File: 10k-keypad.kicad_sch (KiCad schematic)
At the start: 59 parts, among them J1 AVR-ISP-6, K1 SW_Push, K10 SW_Push, K2 SW_Push, K3 SW_Push, K4 SW_Push, K5 SW_Push, K6 SW_Push, K7 SW_Push, K8 SW_Push, K9 SW_Push, SW1 SW_Push, U1 ATmega16U2-A, U2 DRV5055A2xDBZxQ1, U3 DRV5055A2xDBZxQ1, U4 DRV5055A2xDBZxQ1, U5 DRV5055A2xDBZxQ1, U6 DRV5055A2xDBZxQ1, Y1 Crystal_GND24_Small

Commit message: hall sensor circuitry
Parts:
- C10, C11, C12, C13, C14, C15, C5, C6, C7, C9: footprint (none) -> Capacitor_SMD:C_0805_2012Metric_Pad1.18x1.45mm_HandSolder
- K10, K6, K7, K8, K9: footprint marbastlib-mx:SW_MX_HS_CPG151101S11_1u -> Hall:SW_MX_HS_CPG151101S11_1u_no_center_piece
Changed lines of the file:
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@@
       (effects (font (size 1.27 1.27)))
     )
-    (property "Footprint" "" (at 67.31 45.72 0)
+    (property "Footprint" "Capacitor_SMD:C_0805_2012Metric_Pad1.18x1.45mm_HandSolder" (at 67.31 45.72 0)
       (effects (font (size 1.27 1.27)) hide)
     )
@@
       (effects (font (size 1.27 1.27)))
     )
-    (property "Footprint" "" (at 149.86 24.13 0)
+    (property "Footprint" "Capacitor_SMD:C_0805_2012Metric_Pad1.18x1.45mm_HandSolder" (at 149.86 24.13 0)
       (effects (font (size 1.27 1.27)) hide)
     )
@@
       (effects (font (size 1.27 1.27)))
     )
-    (property "Footprint" "" (at 123.19 45.72 0)
+    (property "Footprint" "Capacitor_SMD:C_0805_2012Metric_Pad1.18x1.45mm_HandSolder" (at 123.19 45.72 0)
       (effects (font (size 1.27 1.27)) hide)
     )
@@
       (effects (font (size 1.27 1.27)) hide)
     )
-    (property "Footprint" "marbastlib-mx:SW_MX_HS_CPG151101S11_1u" (at 96.52 123.19 0)
+    (property "Footprint" "Hall:SW_MX_HS_CPG151101S11_1u_no_center_piece" (at 96.52 123.19 0)
       (effects (font (size 1.27 1.27)) hide)
     )
@@
       (effects (font (size 1.27 1.27)) hide)
     )
-    (property "Footprint" "marbastlib-mx:SW_MX_HS_CPG151101S11_1u" (at 66.04 123.19 0)
+    (property "Footprint" "Hall:SW_MX_HS_CPG151101S11_1u_no_center_piece" (at 66.04 123.19 0)
       (effects (font (size 1.27 1.27)) hide)
     )
@@
       (effects (font (size 1.27 1.27)))
     )
-    (property "Footprint" "" (at 38.1 24.13 0)
+    (property "Footprint" "Capacitor_SMD:C_0805_2012Metric_Pad1.18x1.45mm_HandSolder" (at 38.1 24.13 0)
       (effects (font (size 1.27 1.27)) hide)
     )
@@
       (effects (font (size 1.27 1.27)))
     )
-    (property "Footprint" "" (at 39.37 45.72 0)
+    (property "Footprint" "Capacitor_SMD:C_0805_2012Metric_Pad1.18x1.45mm_HandSolder" (at 39.37 45.72 0)
       (effects (font (size 1.27 1.27)) hide)
     )
@@
       (effects (font (size 1.27 1.27)))
     )
-    (property "Footprint" "" (at 121.92 24.13 0)
+    (property "Footprint" "Capacitor_SMD:C_0805_2012Metric_Pad1.18x1.45mm_HandSolder" (at 121.92 24.13 0)
       (effects (font (size 1.27 1.27)) hide)
     )
@@
       (effects (font (size 1.27 1.27)))
     )
-    (property "Footprint" "" (at 151.13 45.72 0)
+    (property "Footprint" "Capacitor_SMD:C_0805_2012Metric_Pad1.18x1.45mm_HandSolder" (at 151.13 45.72 0)
       (effects (font (size 1.27 1.27)) hide)
     )
@@
       (effects (font (size 1.27 1.27)) hide)
     )
-    (property "Footprint" "marbastlib-mx:SW_MX_HS_CPG151101S11_1u" (at 50.8 123.19 0)
+    (property "Footprint" "Hall:SW_MX_HS_CPG151101S11_1u_no_center_piece" (at 50.8 123.19 0)
       (effects (font (size 1.27 1.27)) hide)
     )
@@
       (effects (font (size 1.27 1.27)))
     )
-    (property "Footprint" "" (at 93.98 24.13 0)
+    (property "Footprint" "Capacitor_SMD:C_0805_2012Metric_Pad1.18x1.45mm_HandSolder" (at 93.98 24.13 0)
       (effects (font (size 1.27 1.27)) hide)
     )
@@
       (effects (font (size 1.27 1.27)) hide)
     )
-    (property "Footprint" "marbastlib-mx:SW_MX_HS_CPG151101S11_1u" (at 35.56 123.19 0)
+    (property "Footprint" "Hall:SW_MX_HS_CPG151101S11_1u_no_center_piece" (at 35.56 123.19 0)
       (effects (font (size 1.27 1.27)) hide)
     )
@@
       (effects (font (size 1.27 1.27)))
     )
-    (property "Footprint" "" (at 66.04 24.13 0)
+    (property "Footprint" "Capacitor_SMD:C_0805_2012Metric_Pad1.18x1.45mm_HandSolder" (at 66.04 24.13 0)
       (effects (font (size 1.27 1.27)) hide)
     )
@@
       (effects (font (size 1.27 1.27)) hide)
     )
-    (property "Footprint" "marbastlib-mx:SW_MX_HS_CPG151101S11_1u" (at 81.28 123.19 0)
+    (property "Footprint" "Hall:SW_MX_HS_CPG151101S11_1u_no_center_piece" (at 81.28 123.19 0)
       (effects (font (size 1.27 1.27)) hide)
     )
@@
       (effects (font (size 1.27 1.27)))
     )
-    (property "Footprint" "" (at 95.25 45.72 0)
-      (effects (font (size 1.27 1.27)) hide)
-    )
+    (property "Footprint" "Capacitor_SMD:C_0805_2012Metric_Pad1.18x1.45mm_HandSolder" (at 95.25 45.72 0)
+      (effects (font (size 1.27 1.27)) hide)
+    )

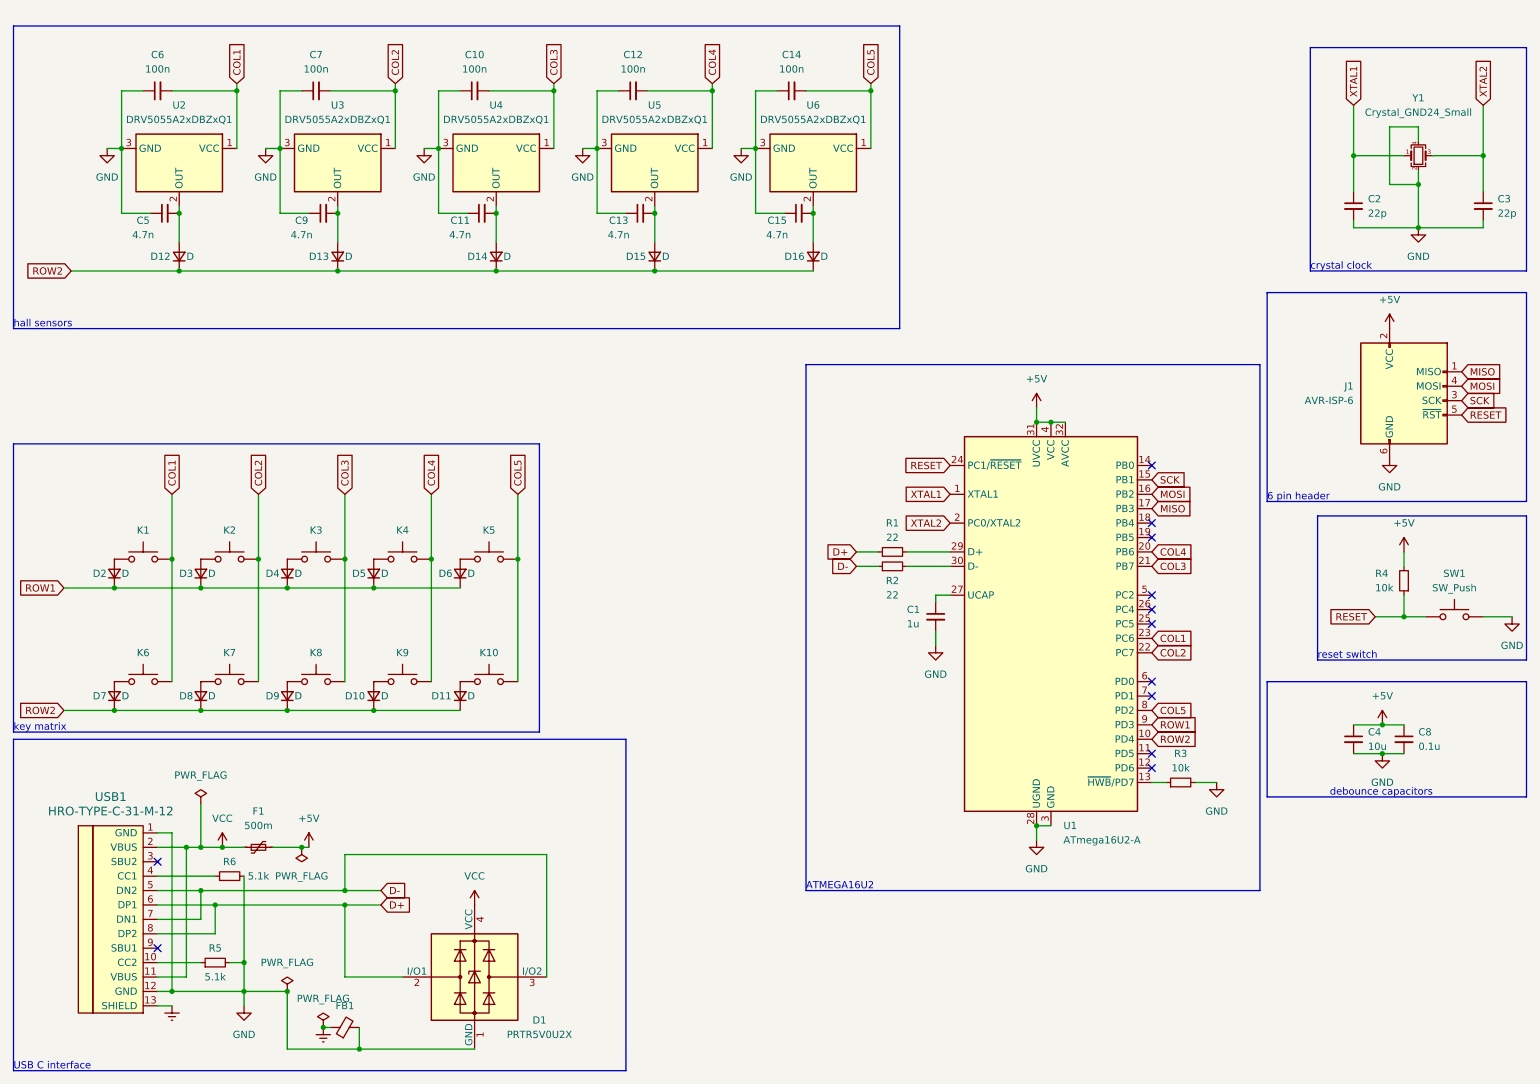
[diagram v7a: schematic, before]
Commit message: fix hall sensor circuitry
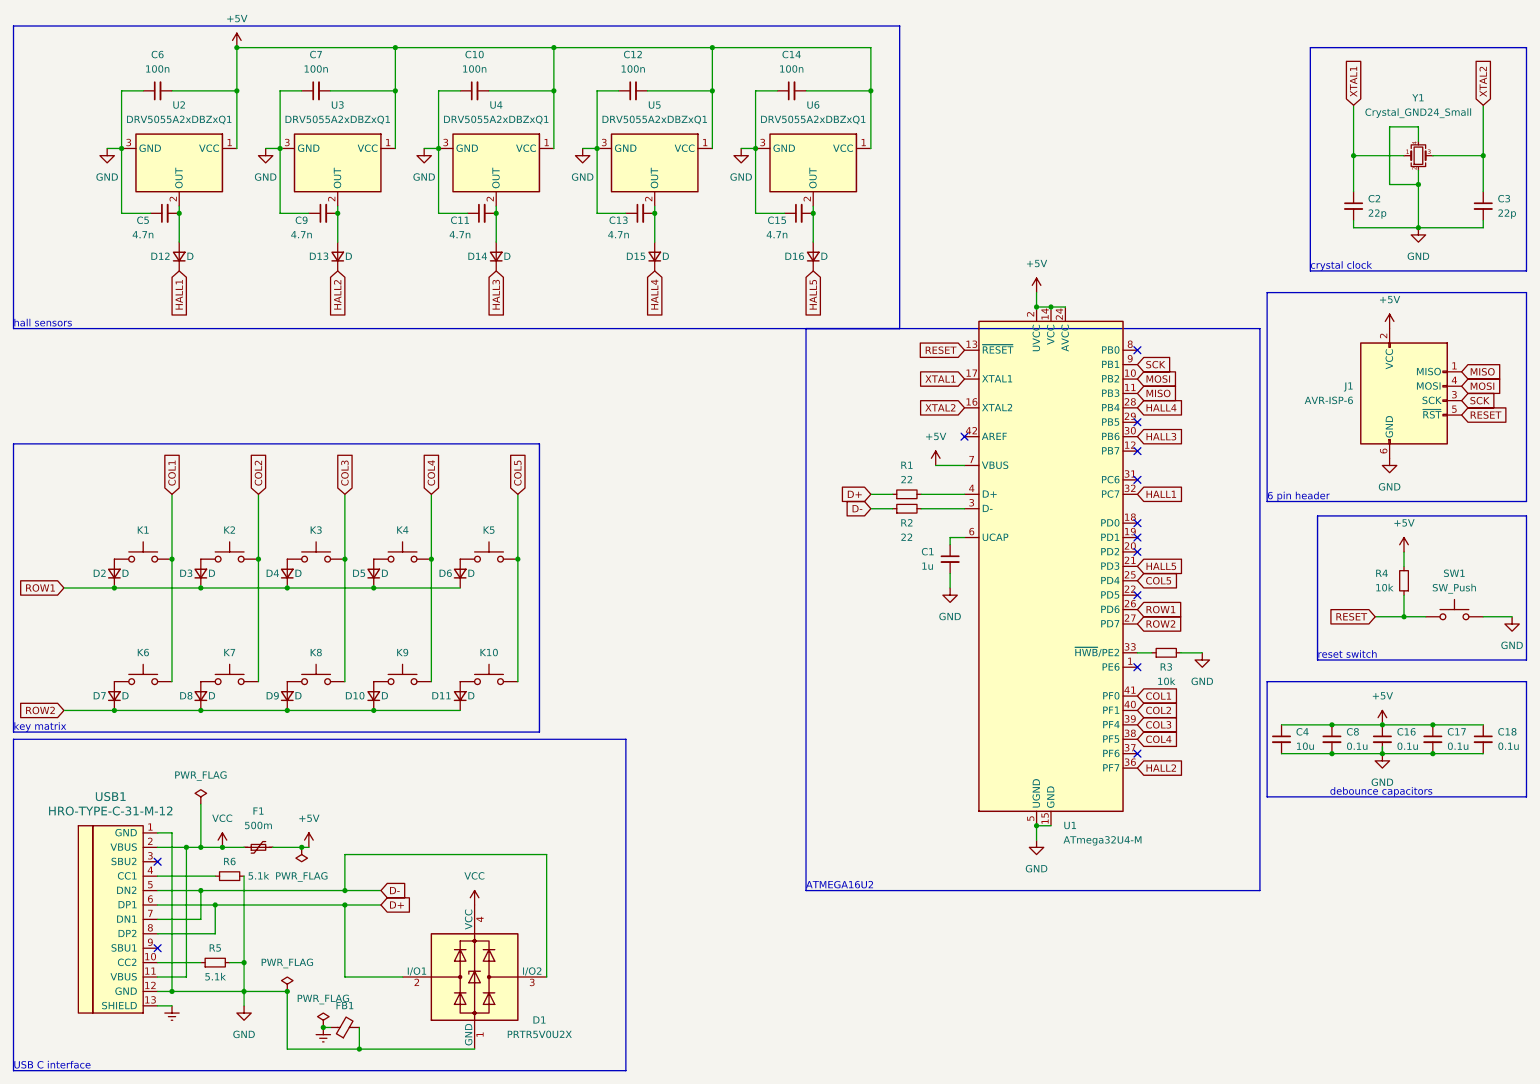
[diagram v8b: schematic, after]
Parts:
- added C16, C17, C18: 0.1u, Capacitor_SMD:C_0805_2012Metric_Pad1.18x1.45mm_HandSolder, symbol Device:C_Small
- U1: value ATmega16U2-A -> ATmega32U4-M; footprint Package_QFP:TQFP-32_7x7mm_P0.8mm -> Package_DFN_QFN:QFN-44-1EP_7x7mm_P0.5mm_EP5.2x5.2mm; symbol MCU_Microchip_ATmega:ATmega16U2-A -> MCU_Microchip_ATmega:ATmega32U4-M
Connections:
- net +5V: now also C10.2, C12.2, C14.2, C6.2, C7.2, U1.14 (VCC), U1.2 (UVCC), U1.24 (AVCC), U1.34 (VCC), U1.44 (AVCC), U1.7 (VBUS), U2.1 (VCC), U3.1 (VCC), U4.1 (VCC), U5.1 (VCC), U6.1 (VCC), C16.1, C17.1, C18.1; no longer U1.31 (UVCC), U1.32 (AVCC), U1.4 (VCC)
- net COL1: now also U1.41 (PF0); no longer C6.2, U1.23 (PC6), U2.1 (VCC)
- net COL2: now also U1.40 (PF1); no longer C7.2, U1.22 (PC7), U3.1 (VCC)
- net COL3: now also U1.39 (PF4); no longer C10.2, U1.21 (PB7), U4.1 (VCC)
- net COL4: now also U1.38 (PF5); no longer C12.2, U1.20 (PB6), U5.1 (VCC)
- net COL5: now also U1.25 (PD4); no longer C14.2, U1.8 (PD2), U6.1 (VCC)
- net GND: now also U1.15 (GND), U1.23 (GND), U1.35 (GND), U1.43 (GND), U1.45 (GND), U1.5 (UGND), C16.2, C17.2, C18.2; no longer U1.28 (UGND), U1.3 (GND)
- net MISO: now also U1.11 (PB3); no longer U1.17 (PB3)
- net MOSI: now also U1.10 (PB2); no longer U1.16 (PB2)
- net RESET: now also U1.13 (~{RESET}); no longer U1.24 (PC1/~{RESET})
- net ROW1: now also U1.26 (PD6); no longer U1.9 (PD3)
- net ROW2: now also U1.27 (PD7); no longer D12.1 (K), D13.1 (K), D14.1 (K), D15.1 (K), D16.1 (K), U1.10 (PD4)
- net SCK: now also U1.9 (PB1); no longer U1.15 (PB1)
- net XTAL1: now also U1.17 (XTAL1); no longer U1.1 (XTAL1)
- net XTAL2: now also U1.16 (XTAL2); no longer U1.2 (PC0/XTAL2)
- net at R3.1: now also U1.33 (~{HWB}/PE2); no longer U1.13 (~{HWB}/PD7)
- net at R1.2: now also U1.4 (D+); no longer U1.29 (D+)
- net at C1.1: now also U1.6 (UCAP); no longer U1.27 (UCAP)
- net at R2.2: now also U1.3 (D-); no longer U1.30 (D-)
- new net HALL1: D12.1 (K), U1.32 (PC7)
- new net HALL2: D13.1 (K), U1.36 (PF7)
- new net HALL3: D14.1 (K), U1.30 (PB6)
- new net HALL4: D15.1 (K), U1.28 (PB4)
- new net HALL5: D16.1 (K), U1.21 (PD3)
- no-connect marks 12 -> 13
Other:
- moved on the sheet: C1, C4, C8, R1, R2, R3
